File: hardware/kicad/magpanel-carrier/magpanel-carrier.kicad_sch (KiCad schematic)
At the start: 38 parts, among them J1 5V IN, J10 EXP, J2 HUB75E PANEL 1, J3 HUB75E PANEL 2, J4 HUB75E PANEL 3, J5 LDR, J6 MIC, J7 ENC, J8 DHT, J9 TOUCH, U1 ESP32-S3-DevKitC-1, U2 74AHCT245, U3 74AHCT245

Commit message: Hardware: fit the KiCad carrier to the parts on hand
- Level shifters are CD74HCT245E in DIP-20 now (socketed footprint),
  stacked in one column with the A pins on the DevKit pin pitch
- DevKit right socket row is 1.0in (25.4 mm): the N16R8 clone on hand
  seated there in the 1:1 paper test; DEVKIT_RIGHT_ROWS switches back
  to the official 0.9in board
- Sensor headers follow the printed pin order of the JSUMO modules.
  The LDR and microphone modules are digital-only: LDR DO -> IO1,
  MIC OUT -> IO42, and R7 pulls the unused analog mic input IO2 to GND
- The 5 V trunk runs below the buffers and enters the DevKit 5V pin
  from underneath the module
- The fab stage also writes a 1:1 placement PDF with a 100 mm scale bar
- Wiring diagram (hardware/gen_schematic.py) and docs follow the actual
  module pinouts

ERC 0, DRC 0 violations, 0 unconnected items, 0 schematic parity issues.

Co-Authored-By: Claude Opus 5.5 <noreply@anthropic.com>
Claude-Session: https://claude.ai/code/session_01CdkdNf8EcXy8Er9VmQyghz
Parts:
- added R7: 100k, Resistor_SMD:R_0805_2012Metric, symbol Device:R
- J6: footprint Connector_PinHeader_2.54mm:PinHeader_1x04_P2.54mm_Vertical -> Connector_PinHeader_2.54mm:PinHeader_1x03_P2.54mm_Vertical; symbol Connector_Generic:Conn_01x04 -> Connector_Generic:Conn_01x03; MPN Pin header 1x4 2.54 mm erkek (Dupont) -> Pin header 1x3 2.54 mm erkek (Dupont)
- U1: MPN ESP32-S3-DevKitC-1-N8R8 / N16R8 klon + 2x 1x22 disi soket (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 -> ESP32-S3 N16R8 klon (YD-ESP32-S3 tipi, siralar arasi 1.0in)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
- U2, U3: value 74AHCT245 -> 74HCT245; footprint Package_SO:SOIC-20W_7.5x12.8mm_P1.27mm -> Package_DIP:DIP-20_W7.62mm_Socket; MPN SN74AHCT245DWR (SOIC-20W) -> CD74HCT245E (PDIP-20) + 20 pin DIP soket
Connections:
- net +3V3: now also J8.3 (Pin_3); no longer J8.1 (Pin_1)
- net GND: now also J8.1 (Pin_1), J9.3 (Pin_3), R7.2; no longer J8.3 (Pin_3), J9.1 (Pin_1)
- net MIC_AO: now also R7.1; no longer J6.1 (Pin_1)
- net MIC_DO: now also J6.1 (Pin_1); no longer J6.4 (Pin_4)
- net TOUCH_OUT: now also J9.1 (Pin_1); no longer J9.3 (Pin_3)
- net LDR_AO renamed LDR_OUT
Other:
- note added: "-/OUT/+; OUT -> IO47"
- note added: "3 SEVIYE DONUSTURUCU 3.3 V -> 5 V (2x 74HCT245)"
- note added: "CLK/DT/SW -> IO41/40/39"
- note added: "DHT11 (JSUMO 15579)"
- note added: "Enkoder KY-040 (JSUMO)"
- note added: "Genisleme (UART0/I2C)"
- note added: "IO43, IO44, IO38"
- note added: "LDR karti (JSUMO 16067)"
- note added: "Mikrofon (JSUMO 15771)"
- note added: "OUT/GND/VCC; OUT -> IO42"
- note added: "Pin sirasi eldeki modullerin baskisiyla ayni; PCB uzerinde her pin etiketli. LDR ve mikrofon modulleri yalniz dijital cikisli. Baglanmamis sensor zararsiz."
- note added: "SIG/VCC/GND; SIG -> IO21"
- note added: "Sag soket 1.0in (25.4 mm; YD-ESP32-S3 tipi N16R8 klon). Resmi kart: 0.9in. Anten (ust) kart kenarindan tasar; USB (alt) kart kenarinda. Kullanilmayan: IO0/45/46 strapping, IO35-37 OPI PSRAM, IO19/20 USB, IO48 (klon RGB LED)."
- note added: "TTP223B (JSUMO 17538)"
- note added: "VCC/GND/DO; DO -> IO1"
- note removed: "3 SEVIYE DONUSTURUCU 3.3 V -> 5 V (2x 74AHCT245)"
- note removed: "AO -> IO1 (ADC1_CH0)"
- note removed: "AO -> IO2, DO -> IO42"
- note removed: "CLK/DT/SW -> IO41/IO40/IO39"
- note removed: "DATA -> IO47"
- note removed: "DHT11 Temperature & Humidity (JSUMO 15579)"
- note removed: "Genisleme (UART0/ileride I2C)"
- note removed: "IO43, IO44, IO38 (v1.1 RGB LED)"
- note removed: "KY-040 Mechanic Encoder"
- note removed: "LDR Sensor Board (JSUMO 16067)"
- note removed: "Microphone Sound Sensor (JSUMO 15771)"
- note removed: "OUT -> IO21"
- note removed: "Pin sirasi yaygin modul baskisini izler; PCB uzerinde her pin etiketli. Baglanmamis sensor zararsiz (firmware: dokunmatik pull-down, enkoder pull-up)."
- note removed: "Sag soket iki sirali: 0.9in (resmi Espressif) / 1.0in (N16R8 klonlari). Anten (ust) kart kenarindan tasar; USB (alt) kart kenarinda. Kullanilmayan: IO0/45/46 strapping, IO35-37 OPI PSRAM, IO19/20 USB, IO48 (klon RGB LED)."
- note removed: "TTP223B Digital Touch (JSUMO 17538)"

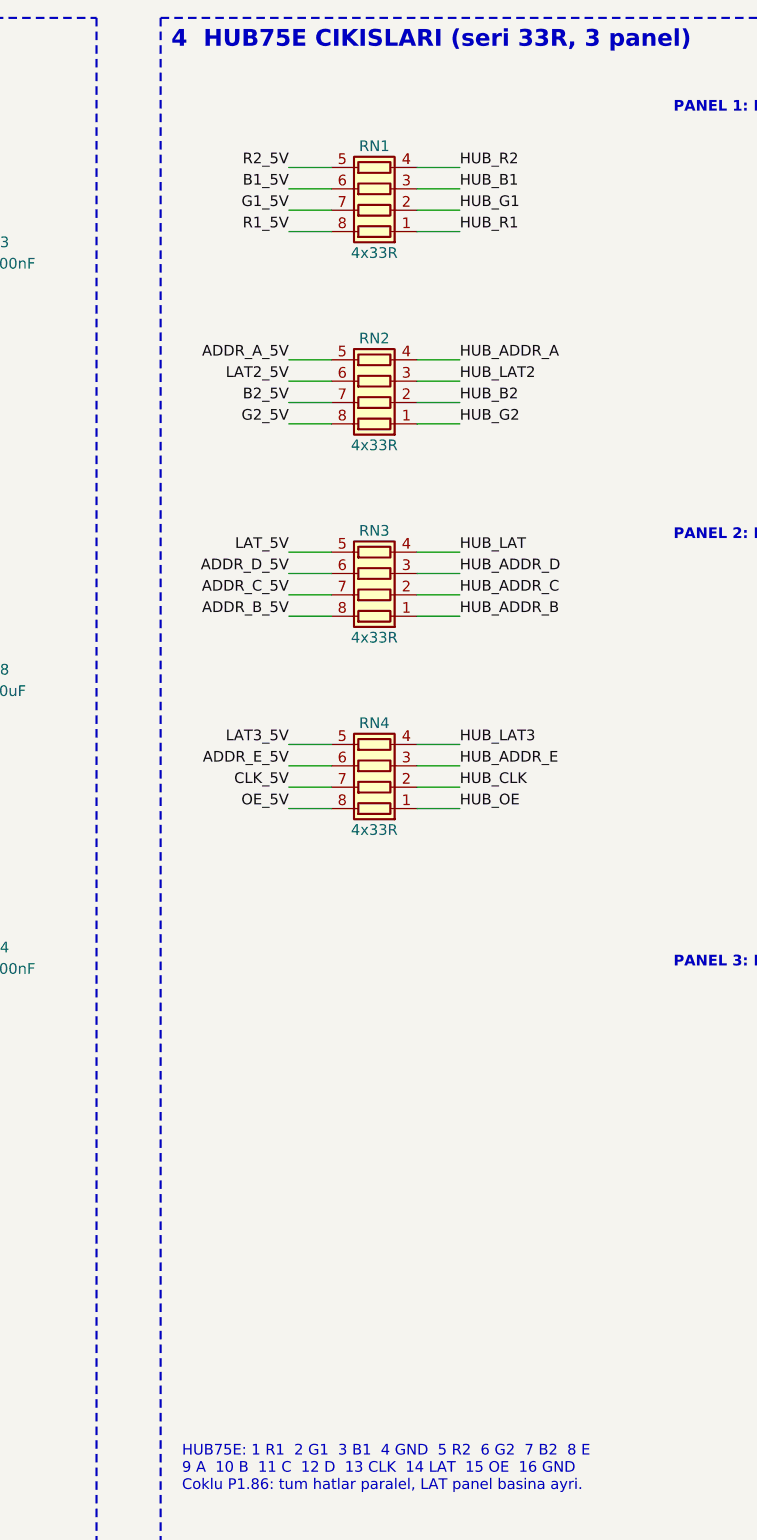
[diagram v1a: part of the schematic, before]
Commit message: Hardware: make the KiCad carrier hand-solder friendly (v1.2)
- Replace the four 4x0603 resistor arrays (0.35 mm between pads) with
  16 discrete 0805 33R resistors (R10-R25) in one column, each in line
  with its 74HCT245 B pin (1.14 mm between neighbouring pads).
- Use HandSolder footprints for every SMD part and LongPads DIP sockets.
- Add a 0.5 mm courtyard clearance DRC rule. v1.1 had 13 violations
  (tightest 0.16 mm); v1.2 has none (tightest 0.58 mm).
- Widen the gaps between the HUB75 box headers from 2.4 mm to 3.8 mm and
  move the SMD parts under the DevKit 4.5 mm away from the socket rows.
- Re-lay the 5 V input block; tie the TVS anode straight to the input
  GND with a locked wide track.
- Seed KiCad's UUID generator so regenerated files are reproducible.
- Document the assembly order and the first power-on check.

Co-Authored-By: Claude Opus 5.5 <noreply@anthropic.com>
Claude-Session: https://claude.ai/code/session_01CdkdNf8EcXy8Er9VmQyghz
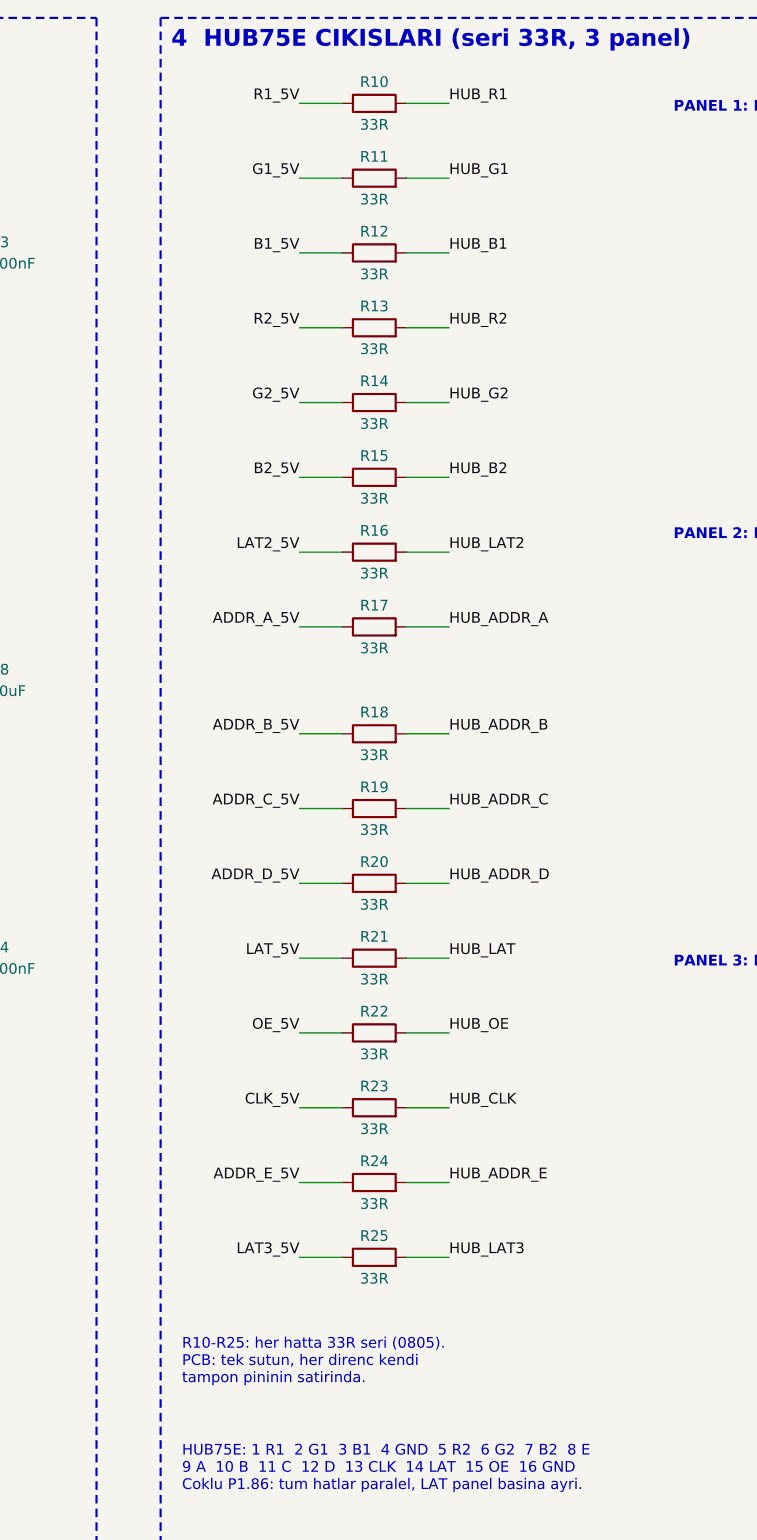
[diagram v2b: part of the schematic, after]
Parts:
- removed RN1, RN2, RN3, RN4: 4x33R, Resistor_SMD:R_Array_Convex_4x0603, symbol Device:R_Pack04
- added R10, R11, R12, R13, R14, R15, R16, R17, R18, R19, R20, R21, R22, R23, R24, R25: 33R, Resistor_SMD:R_0805_2012Metric_Pad1.20x1.40mm_HandSolder, symbol Device:R
- C2, C3, C4, C5, C6, C7, C8: footprint Capacitor_SMD:C_0805_2012Metric -> Capacitor_SMD:C_0805_2012Metric_Pad1.18x1.45mm_HandSolder
- D1: footprint Diode_SMD:D_SMA -> Diode_SMD:D_SMA_Handsoldering
- D2: footprint LED_SMD:LED_0805_2012Metric -> LED_SMD:LED_0805_2012Metric_Pad1.15x1.40mm_HandSolder
- F1: footprint Fuse:Fuse_1812_4532Metric -> Fuse:Fuse_1812_4532Metric_Pad1.30x3.40mm_HandSolder
- R1, R2, R3, R4, R5, R6, R7: footprint Resistor_SMD:R_0805_2012Metric -> Resistor_SMD:R_0805_2012Metric_Pad1.20x1.40mm_HandSolder
- U2, U3: footprint Package_DIP:DIP-20_W7.62mm_Socket -> Package_DIP:DIP-20_W7.62mm_Socket_LongPads
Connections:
- net ADDR_A_5V: now also R17.1
- net ADDR_B_5V: now also R18.1
- net ADDR_C_5V: now also R19.1
- net ADDR_D_5V: now also R20.1
- net ADDR_E_5V: now also R24.1
- net B1_5V: now also R12.1
- net B2_5V: now also R15.1
- net CLK_5V: now also R23.1
- net G1_5V: now also R11.1
- net G2_5V: now also R14.1
- net HUB_ADDR_A: now also R17.2
- net HUB_ADDR_B: now also R18.2
- net HUB_ADDR_C: now also R19.2
- net HUB_ADDR_D: now also R20.2
- net HUB_ADDR_E: now also R24.2
- net HUB_B1: now also R12.2
- net HUB_B2: now also R15.2
- net HUB_CLK: now also R23.2
- net HUB_G1: now also R11.2
- net HUB_G2: now also R14.2
- net HUB_LAT: now also R21.2
- net HUB_LAT2: now also R16.2
- net HUB_LAT3: now also R25.2
- net HUB_OE: now also R22.2
- net HUB_R1: now also R10.2
- net HUB_R2: now also R13.2
- net LAT2_5V: now also R16.1
- net LAT3_5V: now also R25.1
- net LAT_5V: now also R21.1
- net OE_5V: now also R22.1
- net R1_5V: now also R10.1
- net R2_5V: now also R13.1
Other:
- note added: "R10-R25: her hatta 33R seri (0805). PCB: tek sutun, her direnc kendi tampon pininin satirinda."

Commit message: Hardware: SMT assembly files for Robotistan and JLCPCB with verified LCSC parts
- Add SMT_PARTS: manufacturer, MPN and LCSC number for every SMD part,
  checked against LCSC's product API (all in stock). The schematic
  fields, the JLC BOM and the full BOM now carry them.
- Generate Robotistan's BOM and pick-and-place spreadsheets with the
  columns of their sample files. xlsx.py is a small stdlib writer, so
  the fab stage needs no extra Python package.
- Use the board's lower-left corner as the origin for gerbers, drill
  files and placement files, so all coordinates are positive and line
  up. The routed copper is unchanged; only the aux origin was added.
- Write the project JSON in KiCad's key and net class order so a
  regeneration does not reorder it.
- Document the Robotistan order form choices.

Co-Authored-By: Claude Opus 5.5 <noreply@anthropic.com>
Claude-Session: https://claude.ai/code/session_01CdkdNf8EcXy8Er9VmQyghz
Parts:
- C2, C8: LCSC (none) -> C15850; MPN MLCC 10 uF 16 V X5R 0805 -> CL21A106KAYNNNE; Manufacturer (none) -> Samsung
- C3, C4, C5, C6, C7: LCSC (none) -> C49678; MPN MLCC 100 nF 50 V X7R 0805 -> CC0805KRX7R9BB104; Manufacturer (none) -> YAGEO
- D1: LCSC (none) -> C83329; MPN SMAJ5.0A (400 W, 5 V TVS) -> SMAJ5.0A; Manufacturer (none) -> Littelfuse
- D2: LCSC (none) -> C2297; MPN LED 0805 yesil -> KT-0805G; Manufacturer (none) -> Hubei KENTO
- F1: LCSC (none) -> C89648; MPN Bourns MF-MSMF150-2 (1812, 1.5 A hold) -> MF-MSMF150-2; Manufacturer (none) -> BOURNS
- R1: LCSC (none) -> C17520; MPN 0805 2.2 kOhm 1% -> 0805W8F2201T5E; Manufacturer (none) -> UNI-ROYAL
- R10, R11, R12, R13, R14, R15, R16, R17, R18, R19, R20, R21, R22, R23, R24, R25: LCSC (none) -> C17634; MPN 0805 33 Ohm 1% -> 0805W8F330JT5E; Manufacturer (none) -> UNI-ROYAL
- R2, R3, R4, R5, R6: LCSC (none) -> C17414; MPN 0805 10 kOhm 1% -> 0805W8F1002T5E; Manufacturer (none) -> UNI-ROYAL
- R7: LCSC (none) -> C17407; MPN 0805 100 kOhm 1% -> 0805W8F1003T5E; Manufacturer (none) -> UNI-ROYAL

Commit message: Hardware: use 10k for R7 so every SMD part is in Robotistan's stock
Robotistan's BOM check reported the 100k part (C17407, an LCSC "(SMT)"
listing) as out of stock. R7 only pulls the unused IO2 input low, so its
value does not matter. It now uses the same 10k part as R2-R6 and the
assembly BOM shrinks to 8 lines. Placement and copper are unchanged.

Also pin the creation time KiCad writes into gerber and drill files to
DATE, so the gerber zip only changes when the board does.

Co-Authored-By: Claude Opus 5.5 <noreply@anthropic.com>
Claude-Session: https://claude.ai/code/session_01CdkdNf8EcXy8Er9VmQyghz
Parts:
- R7: value 100k -> 10k; LCSC C17407 -> C17414; MPN 0805W8F1003T5E -> 0805W8F1002T5E
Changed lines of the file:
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@@
 			(effects (font (size 1.27 1.27)) (justify left))
 		)
-		(property "Value" "100k"
+		(property "Value" "10k"
 			(at 78.74 267.97 0)
 			(effects (font (size 1.27 1.27)) (justify left))
@@
 			(effects (font (size 1.27 1.27)) (hide yes))
 		)
-		(property "MPN" "0805W8F1003T5E"
+		(property "MPN" "0805W8F1002T5E"
 			(at 76.2 266.7 0)
 			(effects (font (size 1.27 1.27)) (hide yes))
@@
 			(effects (font (size 1.27 1.27)) (hide yes))
 		)
-		(property "LCSC" "C17407" (at 76.2 266.7 0) (effects (font (size 1.27 1.27)) (hide yes)))
+		(property "LCSC" "C17414" (at 76.2 266.7 0) (effects (font (size 1.27 1.27)) (hide yes)))
 		(pin "1")
 		(pin "2")
